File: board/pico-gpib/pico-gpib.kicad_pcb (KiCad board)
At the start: 2 copper layers, 65 x 45 mm, 68 parts, among them J1 GPIB, J2 USB_B_Micro, J3 RPI_GPIO, J4 Debug, U1 RP2040, U2 SN75160BDW, U3 SN75162BDW, U4 W25Q128JVS, U5 NCP1117-3.3, U6 CAT24C32, Y1 12M10PI/XT324-10/20

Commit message: Route more stuff.
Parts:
- moved C18 6.99 mm to (120.0, 96.0)
- moved C19 6.99 mm to (121.0, 96.0)
- moved U5 6.99 mm to (126.1, 96.0)
- moved R4 4.70 mm to (132.6, 93.5), turned to 0 degrees
- moved U4 3.56 mm to (135.8, 96.9)
- moved C15 3.11 mm to (141.0, 95.5), turned to 270 degrees
- moved C10 0.52 mm to (134.7, 92.2), turned to 270 degrees
- moved C8 0.46 mm to (139.1, 92.2), turned to 270 degrees
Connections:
- J4 pad 1: /DEBUG_RUN -> /DEBUG_DATA
- J4 pad 2: /DEBUG_CLOCK -> GND
- J4 pad 3: /DEBUG_DATA -> /DEBUG_CLOCK
- U1 pad 26: /DEBUG_RUN -> Net-(U1-Pad26)
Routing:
- net /DEBUG_CLOCK: track 0.00 -> 54.2 mm, vias 0 -> 1
- net /DEBUG_DATA: track 0.00 -> 47.4 mm, vias 0 -> 1
- net +5V: track 25.5 -> 56.0 mm, vias 0 -> 2
- net /SC: track 0.00 -> 27.9 mm
- net +3V3: track 53.2 -> 69.5 mm, vias 0 -> 3
- net /FLASH_D0: track 0.00 -> 14.9 mm, vias 0 -> 2
- net /FLASH_CLK: track 0.00 -> 14.2 mm, vias 0 -> 2
- net /TE: track 19.9 -> 33.5 mm
- net /FLASH_D3: track 0.00 -> 13.4 mm, vias 0 -> 2
- net /FLASH_D2: track 0.00 -> 11.1 mm
- net /FLASH_D1: track 0.00 -> 9.78 mm
- net GND: track 116.0 -> 123.9 mm, vias 11 -> 18
- net /FLASH_~CS: track 0.00 -> 6.49 mm
- net +1V1: track 14.9 -> 18.2 mm

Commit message: Route almost everything.
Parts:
- moved C15 2.67 mm to (143.6, 95.5)
- moved U4 2.67 mm to (138.4, 96.9)
- moved R4 2.16 mm to (134.7, 93.5)
- moved C10 0.25 mm to (134.7, 92.5), turned to 180 degrees
- moved C8 0.13 mm to (139.2, 92.2)
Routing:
- net +3V3: track 69.5 -> 103.8 mm, vias 3 -> 6
- net Net-(U1-Pad11): track 0.00 -> 10.4 mm
- net Net-(U1-Pad12): track 0.00 -> 10.3 mm
- net Net-(U1-Pad9): track 0.00 -> 9.92 mm
- net Net-(U1-Pad8): track 0.00 -> 9.88 mm
- net Net-(U1-Pad7): track 0.00 -> 9.84 mm
- net Net-(U1-Pad3): track 0.00 -> 9.81 mm
- net Net-(U1-Pad6): track 0.00 -> 9.80 mm
- net Net-(U1-Pad5): track 0.00 -> 9.76 mm
- net Net-(U1-Pad4): track 0.00 -> 9.72 mm
- net Net-(U1-Pad2): track 0.00 -> 9.62 mm
- net GND: track 123.9 -> 132.3 mm, vias 18 -> 21
- net /TE: track 33.5 -> 35.7 mm, vias 0 -> 2
- net /SC: track 27.9 -> 29.3 mm, vias 0 -> 2
- net /DEBUG_DATA: track 47.4 -> 48.8 mm
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- removed copper zone on F.Cu, net Earth_Protective

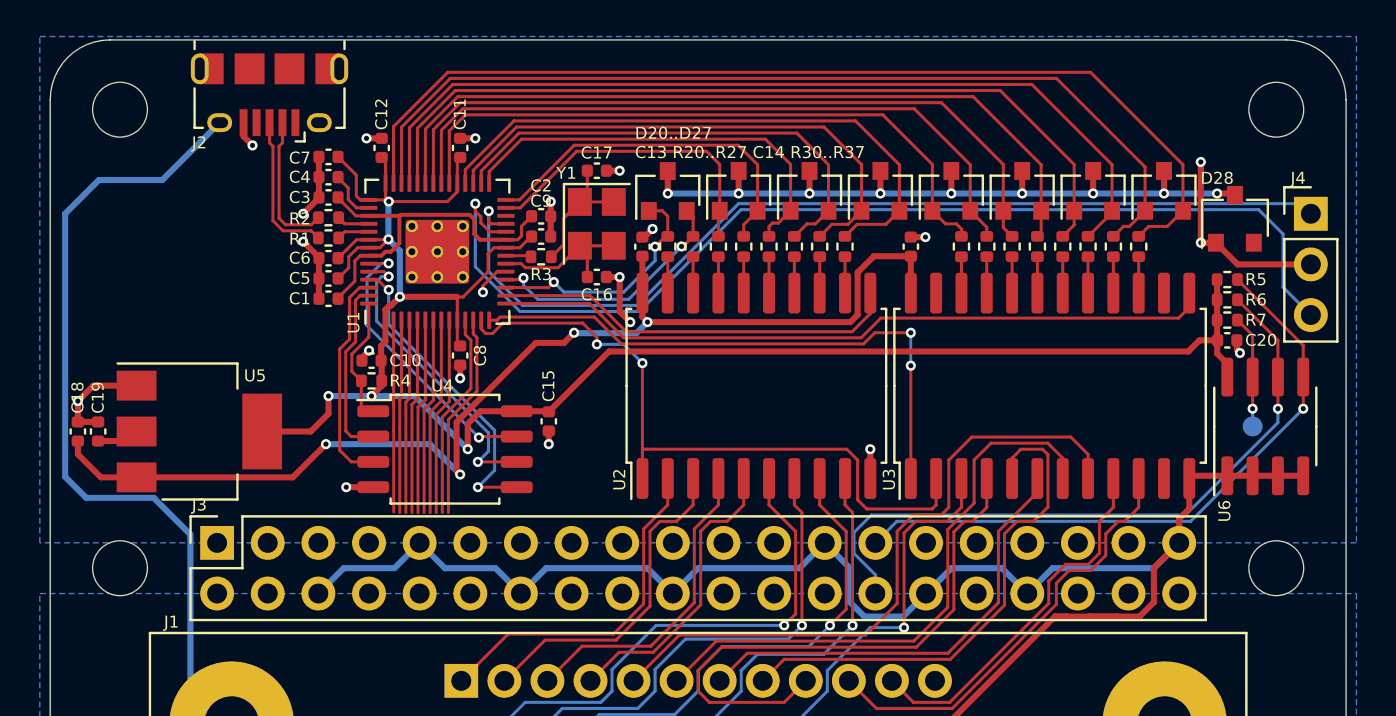
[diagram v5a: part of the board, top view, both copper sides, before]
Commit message: Add labels and test points.
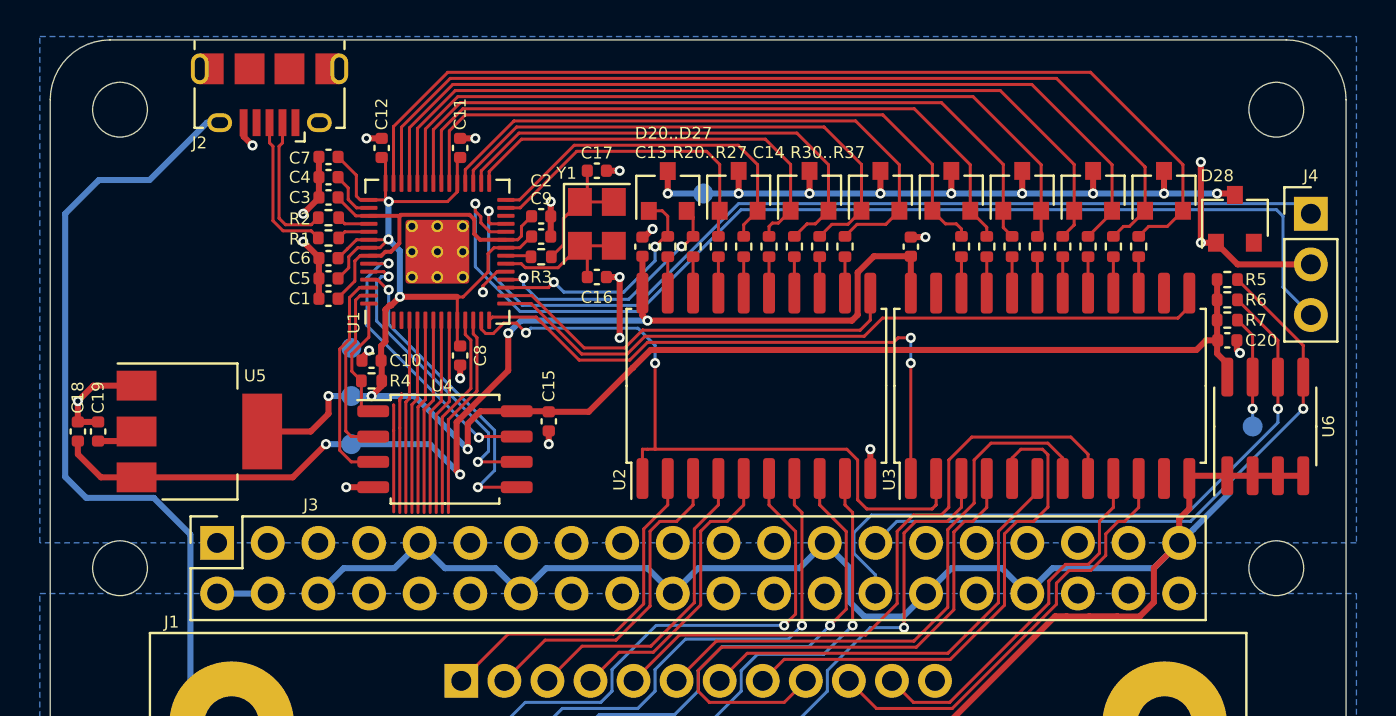
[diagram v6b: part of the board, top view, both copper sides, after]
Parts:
- added OSHW: LOGO, local:OSHW, B.Cu at (173.7, 79.0)
- added TP2: TestPoint, TestPoint:TestPoint_Pad_D1.0mm, B.Cu at (133.7, 96.6)
- added TP3: TestPoint, TestPoint:TestPoint_Pad_D1.0mm, B.Cu at (133.7, 94.2)
- added TP4: TestPoint, TestPoint:TestPoint_Pad_D1.0mm, B.Cu at (151.4, 84.1)
- added TP5: TestPoint, TestPoint:TestPoint_Pad_D1.0mm, B.Cu at (133.7, 91.8)
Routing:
- net Net-(U1-Pad2): track 9.62 -> 5.37 mm
- net GND: track 132.3 -> 136.5 mm
- net Net-(U1-Pad3): track 9.81 -> 6.11 mm
- net Net-(J3-Pad2): track 0.00 -> 2.54 mm
- net +5V: track 57.1 -> 58.1 mm
- net /~PE: track 20.4 -> 21.3 mm
- net /DC: track 36.3 -> 37.0 mm
- net /DEBUG_CLOCK: track 55.3 -> 55.9 mm
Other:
- board text added: "+2V5"
- board text added: "+3V3"
- board text added: "+5V"
- board text added: "ATN"
- board text added: "DAV"
- board text added: "DIO1"
- board text added: "DIO2"
- board text added: "DIO3"
- board text added: "DIO4"
- board text added: "DIO5"
- board text added: "DIO6"
- board text added: "DIO7"
- board text added: "DIO8"
- board text added: "EOI"
- board text added: "GND"
- board text added: "IDSC"
- board text added: "IDSD"
- board text added: "IDWP"
- board text added: "IFC"
- board text added: "PE"
- board text added: "Pico-GPIB v0.1"
- board text added: "REN"
- board text added: "SRQ"
- board text added: "SWC"
- board text added: "SWD"
- board text added: "https://github.com/elemecca/rpi-gpib Licensed under CERN OHL v1.2"
- board text added: "~DAC"
- board text added: "~RFD"

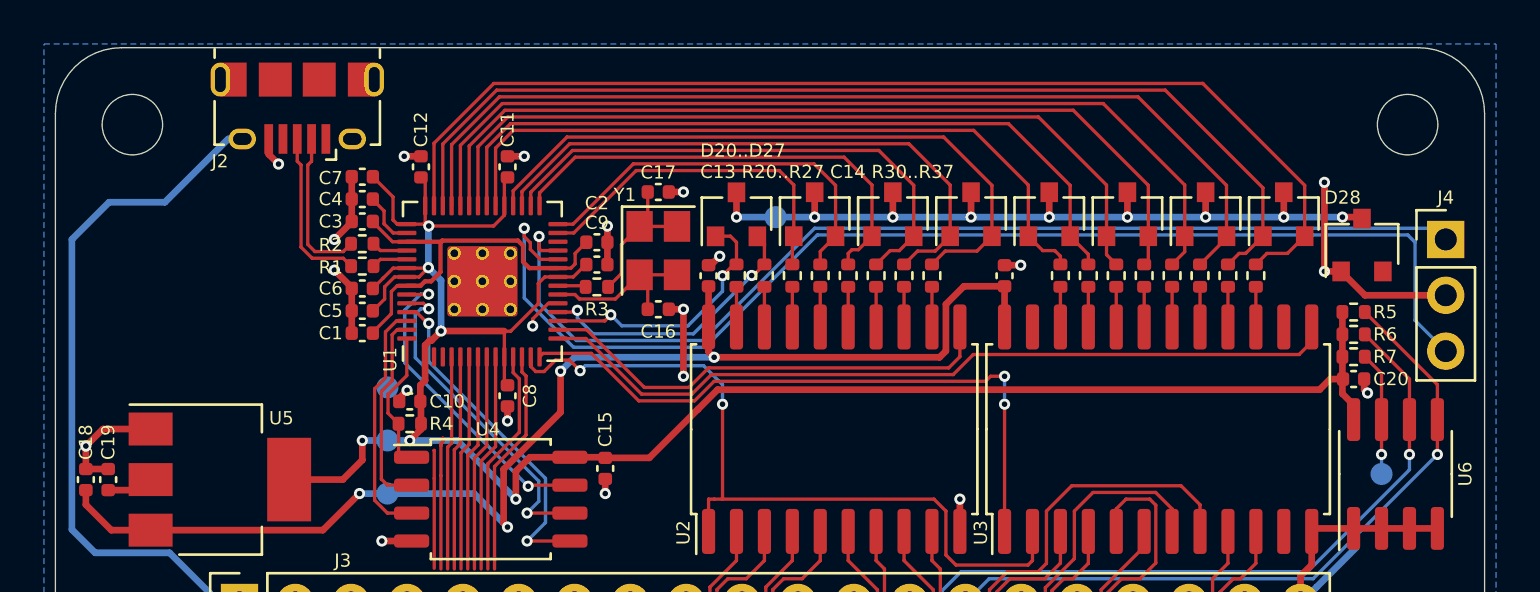
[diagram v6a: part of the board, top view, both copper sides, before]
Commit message: Renumber caps to make more sense.
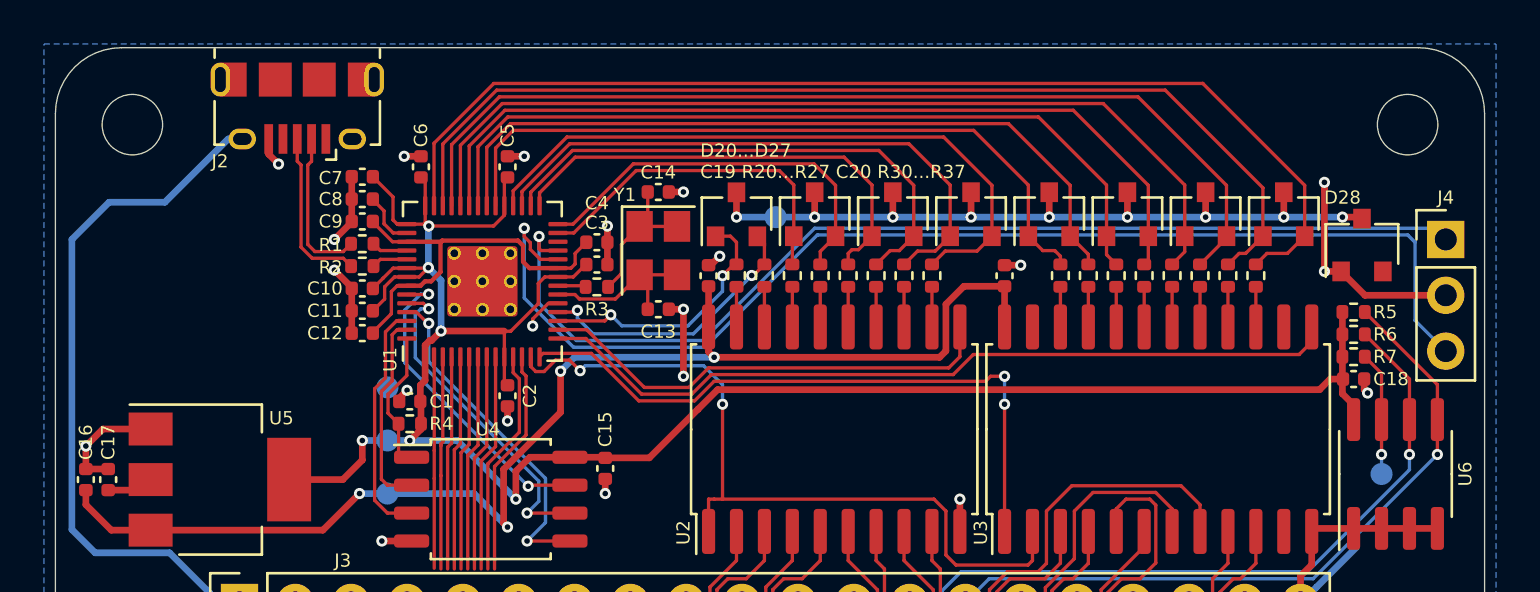
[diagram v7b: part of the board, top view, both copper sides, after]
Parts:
- renumbered C10 to C1, C6 to C10, C5 to C11, C1 to C12, C16 to C13, C17 to C14, C18 to C16, C19 to C17, C20 to C18, C13 to C19, C8 to C2, C14 to C20, C9 to C3, C2 to C4, C11 to C5, C12 to C6, C4 to C8, C3 to C9, R2 to R1, R1 to R2
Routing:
- net Net-(U1-Pad2): track 5.37 -> 9.62 mm
- net Net-(U1-Pad3): track 6.11 -> 9.81 mm
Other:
- board text added: "D20...D27 C19 R20...R27 C20 R30...R37"
- board text removed: "D20..D27 C13 R20..R27 C14 R30..R37"

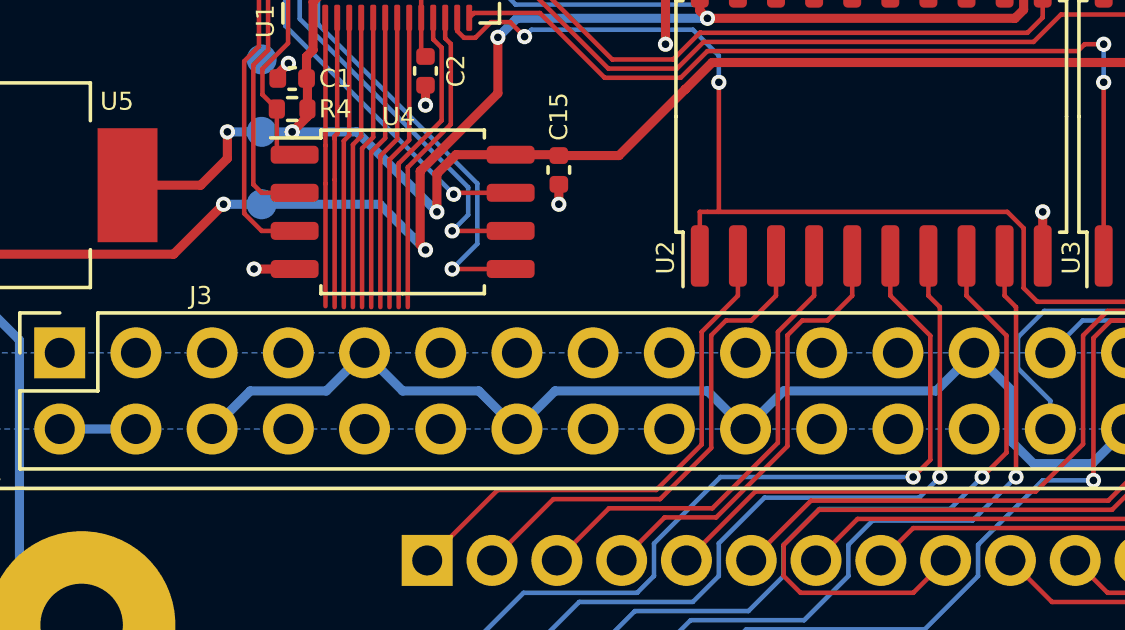
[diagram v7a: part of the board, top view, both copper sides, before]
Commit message: Clean up pico schematic.
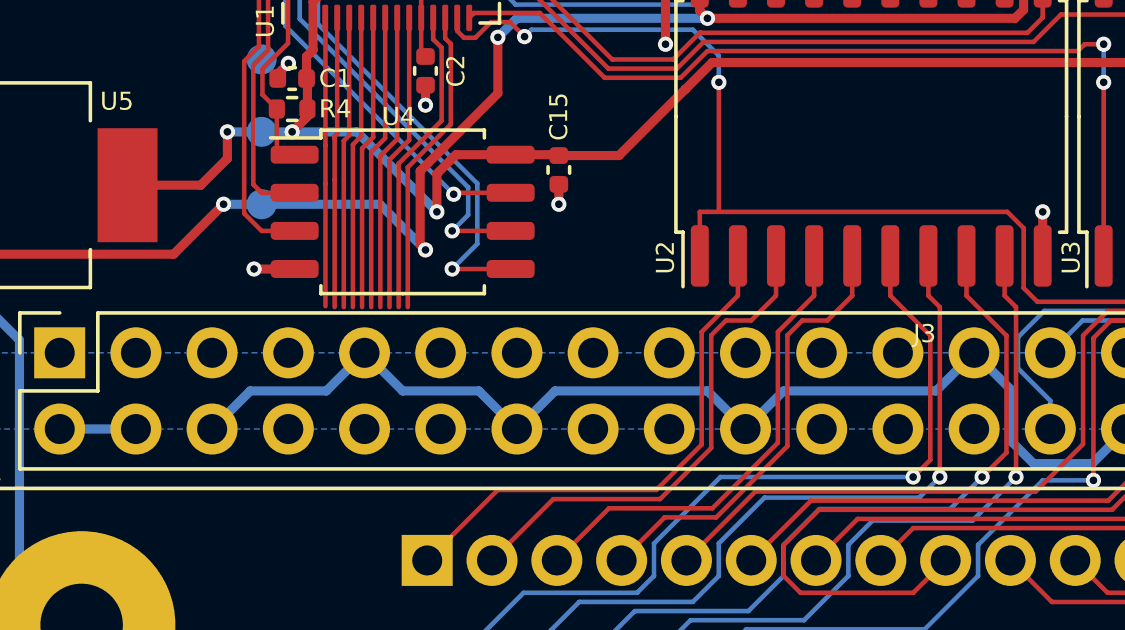
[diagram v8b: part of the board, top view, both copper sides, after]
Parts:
- J3: value RPI_GPIO -> RasPi_Header_40W; footprint lib:PinSocket_2x20_P2.54mm_Vertical_Centered_Anchor -> local:PinSocket_2x20_P2.54mm_Vertical_Centered_Anchor
- R20, R21, R22, R23, R24, R25, R26, R27, R30, R31, R32, R33, R34, R35, R36, R37: value R -> 1k
- moved J3 24.2 mm to (151.1, 102.9)
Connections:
- net Net-(J3-Pad2) renamed +5VP
